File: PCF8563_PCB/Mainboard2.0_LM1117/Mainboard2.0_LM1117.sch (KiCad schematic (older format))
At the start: 40 parts, among them J1 USB_B, J2 CONN_01X03, J3 CONN_01X03, J4 CONN_01X02, J5 CONN_01X02, J6 SD_Card, Q1 BC847, Q2 BC847, SW1 SW_DIP_x01, U1 FT232RL, U2 ESP-12E, U3 PCF8563, U4 LM1117-3.3, Y1 Crystal

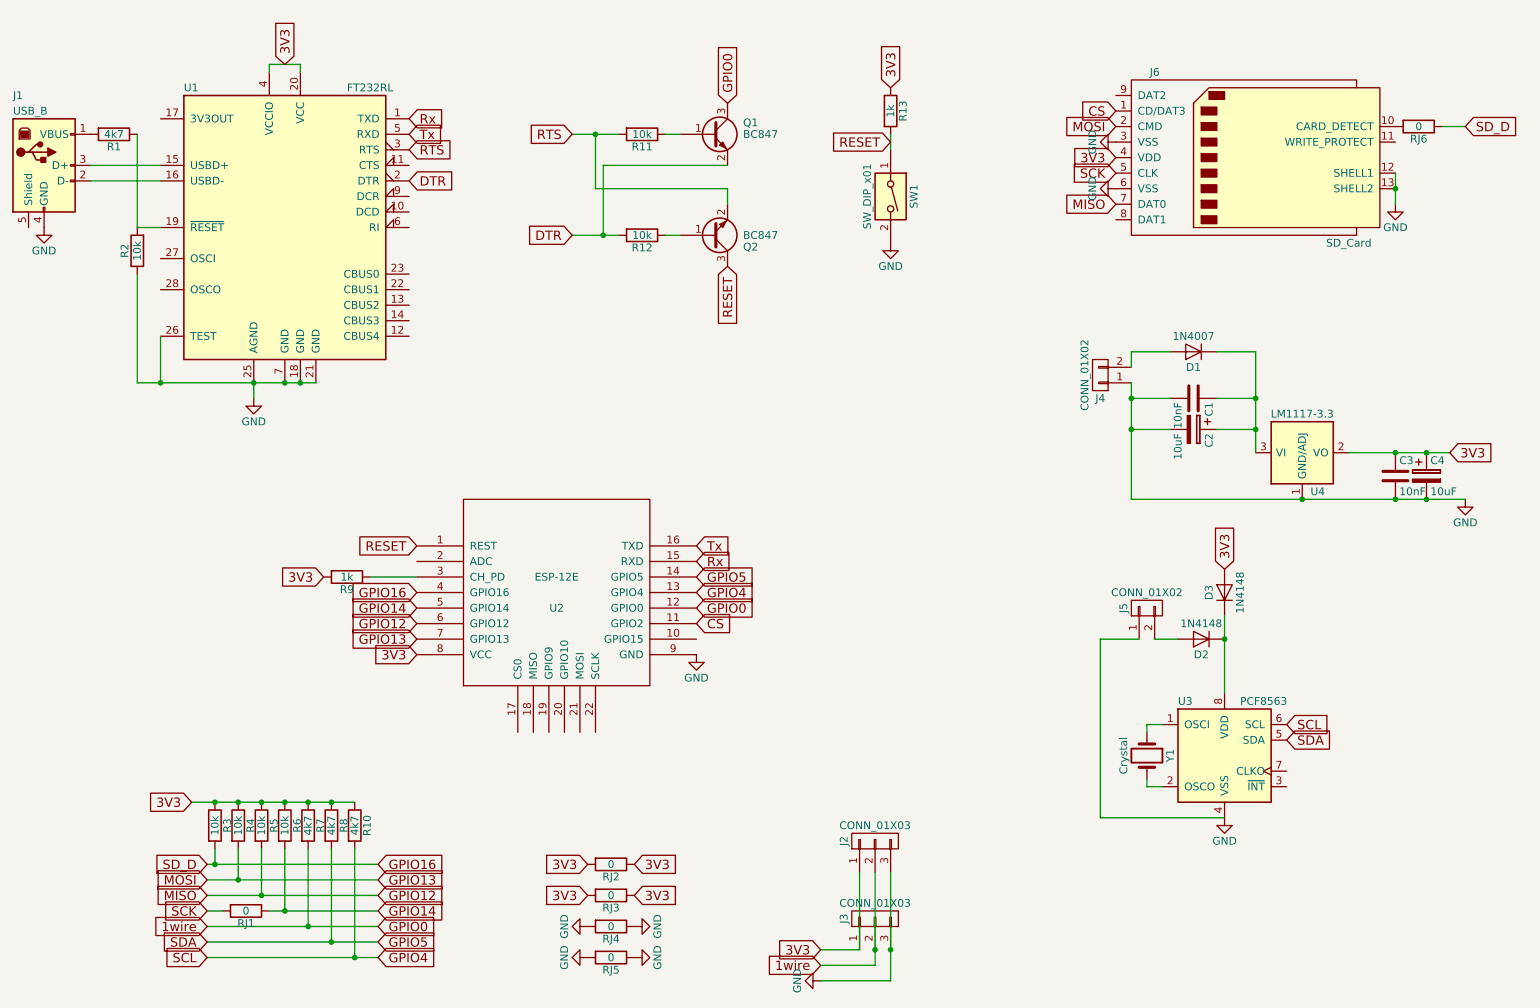
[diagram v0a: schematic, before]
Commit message: PCB work
Need to remove 1.1 files from 2.0 folder
Fixed component enumeration so PCB rework will be easier
Still need to finish new PCB
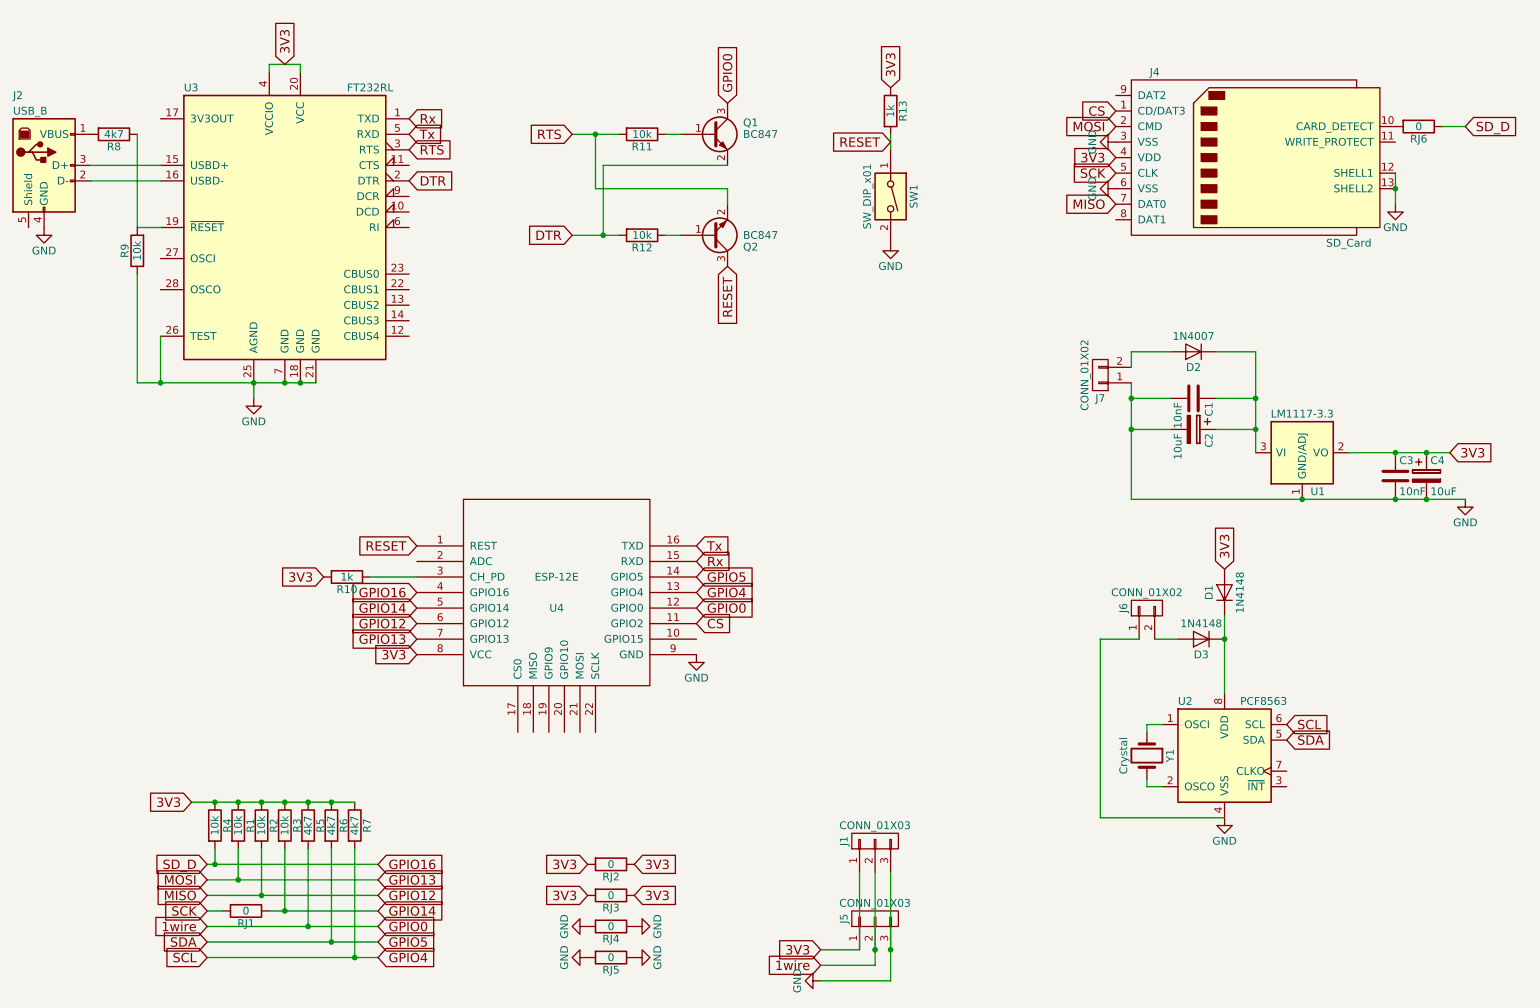
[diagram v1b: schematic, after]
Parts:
- renumbered D3 to D1, D1 to D2, D2 to D3, J2 to J1, J1 to J2, J6 to J4, J3 to J5, J5 to J6, J4 to J7, R4 to R1, R9 to R10, R5 to R2, R6 to R3, R3 to R4, R7 to R5, R8 to R6, R10 to R7, R1 to R8, R2 to R9, U4 to U1, U3 to U2, U1 to U3, U2 to U4
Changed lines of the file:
@@
 LIBS:valves
 LIBS:ESP8266
-LIBS:74xgxx
-LIBS:ac-dc
-LIBS:actel
-LIBS:allegro
-LIBS:Altera
-LIBS:analog_devices
-LIBS:battery_management
-LIBS:bbd
-LIBS:bosch
-LIBS:brooktre
-LIBS:cmos_ieee
-LIBS:dc-dc
-LIBS:diode
-LIBS:elec-unifil
-LIBS:ESD_Protection
-LIBS:ftdi
-LIBS:gennum
-LIBS:graphic_symbols
-LIBS:hc11
-LIBS:infineon
-LIBS:intersil
-LIBS:ir
-LIBS:Lattice
-LIBS:leds
-LIBS:LEM
-LIBS:maxim
-LIBS:mechanical
-LIBS:microchip_dspic33dsc
-LIBS:microchip_pic10mcu
-LIBS:microchip_pic12mcu
-LIBS:microchip_pic16mcu
-LIBS:microchip_pic18mcu
-LIBS:microchip_pic24mcu
-LIBS:microchip_pic32mcu
-LIBS:modules
-LIBS:motor_drivers
-LIBS:motors
-LIBS:msp430
-LIBS:nordicsemi
-LIBS:nxp
-LIBS:nxp_armmcu
-LIBS:onsemi
-LIBS:Oscillators
-LIBS:Power_Management
-LIBS:powerint
-LIBS:pspice
-LIBS:references
-LIBS:relays
-LIBS:rfcom
-LIBS:RFSolutions
-LIBS:sensors
-LIBS:silabs
-LIBS:stm8
-LIBS:stm32
-LIBS:supertex
-LIBS:switches
-LIBS:transf
-LIBS:triac_thyristor
-LIBS:ttl_ieee
-LIBS:video
-LIBS:wiznet
-LIBS:Worldsemi
-LIBS:Xicor
-LIBS:zetex
-LIBS:Zilog
 LIBS:Mainboard2.0_LM1117-cache
 EELAYER 25 0
@@
 GPIO16
 $Comp
-L R R7
+L R R5
 U 1 1 591DCE97
 P 2550 6200
-F 0 "R7" V 2630 6200 50  0000 C CNN
+F 0 "R5" V 2630 6200 50  0000 C CNN
 F 1 "4k7" V 2550 6200 50  0000 C CNN
 F 2 "Resistors_SMD:R_1206_HandSoldering" V 2480 6200 50  0001 C CNN
@@
 $EndComp
 $Comp
-L R R8
+L R R6
 U 1 1 591DCEFA
 P 2700 6200
-F 0 "R8" V 2780 6200 50  0000 C CNN
+F 0 "R6" V 2780 6200 50  0000 C CNN
 F 1 "4k7" V 2700 6200 50  0000 C CNN
 F 2 "Resistors_SMD:R_1206_HandSoldering" V 2630 6200 50  0001 C CNN
@@
 $EndComp
 $Comp
-L R R10
+L R R7
 U 1 1 591DCF1C
 P 2850 6200
-F 0 "R10" V 2930 6200 50  0000 C CNN
+F 0 "R7" V 2930 6200 50  0000 C CNN
 F 1 "4k7" V 2850 6200 50  0000 C CNN
 F 2 "Resistors_SMD:R_1206_HandSoldering" V 2780 6200 50  0001 C CNN
@@
 $EndComp
 $Comp
-L CONN_01X03 J3
+L CONN_01X03 J5
 U 1 1 591DD18C
 P 6200 6800
-F 0 "J3" H 6200 7000 50  0000 C CNN
+F 0 "J5" H 6200 7000 50  0000 C CNN
 F 1 "CONN_01X03" V 6300 6800 50  0000 C CNN
 F 2 "Pin_Headers:Pin_Header_Straight_1x03_Pitch2.54mm_SMD_Pin1Left" H 6200 6800 50  0001 C CNN
@@
 $EndComp
 $Comp
-L CONN_01X03 J2
+L CONN_01X03 J1
 U 1 1 591DD1E5
 P 6200 6300
-F 0 "J2" H 6200 6500 50  0000 C CNN
+F 0 "J1" H 6200 6500 50  0000 C CNN
 F 1 "CONN_01X03" V 6300 6300 50  0000 C CNN
 F 2 "Pin_Headers:Pin_Header_Straight_1x03_Pitch2.54mm_SMD_Pin1Left" H 6200 6300 50  0001 C CNN
@@
 $EndComp
 $Comp
-L SD_Card J6
+L SD_Card J4
 U 1 1 591DD53A
 P 8650 1900
-F 0 "J6" H 8000 2450 50  0000 C CNN
+F 0 "J4" H 8000 2450 50  0000 C CNN
 F 1 "SD_Card" H 9250 1350 50  0000 C CNN
 F 2 "Moje:SDCARD-STANDARD" H 8850 2250 50  0001 C CNN
@@
 MISO
 $Comp
-L R R3
+L R R4
 U 1 1 591DDBFF
 P 1950 6200
-F 0 "R3" V 2030 6200 50  0000 C CNN
+F 0 "R4" V 2030 6200 50  0000 C CNN
 F 1 "10k" V 1950 6200 50  0000 C CNN
 F 2 "Resistors_SMD:R_1206_HandSoldering" V 1880 6200 50  0001 C CNN
@@
 SD_D
 $Comp
-L R R4
+L R R1
 U 1 1 591DE219
 P 2100 6200
-F 0 "R4" V 2180 6200 50  0000 C CNN
+F 0 "R1" V 2180 6200 50  0000 C CNN
 F 1 "10k" V 2100 6200 50  0000 C CNN
 F 2 "Resistors_SMD:R_1206_HandSoldering" V 2030 6200 50  0001 C CNN
@@
 $EndComp
 $Comp
-L R R5
+L R R2
 U 1 1 591DE506
 P 2250 6200
-F 0 "R5" V 2330 6200 50  0000 C CNN
+F 0 "R2" V 2330 6200 50  0000 C CNN
 F 1 "10k" V 2250 6200 50  0000 C CNN
 F 2 "Resistors_SMD:R_1206_HandSoldering" V 2180 6200 50  0001 C CNN
@@
 $EndComp
 $Comp
-L R R6
+L R R3
 U 1 1 591DE541
 P 2400 6200
-F 0 "R6" V 2480 6200 50  0000 C CNN
+F 0 "R3" V 2480 6200 50  0000 C CNN
 F 1 "10k" V 2400 6200 50  0000 C CNN
 F 2 "Resistors_SMD:R_1206_HandSoldering" V 2330 6200 50  0001 C CNN
@@
 3V3
 $Comp
-L PCF8563 U3
+L PCF8563 U2
 U 1 1 591DECCB
 P 8450 5750
-F 0 "U3" H 8150 6100 50  0000 L CNN
+F 0 "U2" H 8150 6100 50  0000 L CNN
 F 1 "PCF8563" H 8550 6100 50  0000 L CNN
 F 2 "Housings_SOIC:SOIC-8_3.9x4.9mm_Pitch1.27mm" H 8450 5750 50  0001 C CNN
@@
 $EndComp
 $Comp
-L D D2
+L D D3
 U 1 1 591DF21A
 P 8300 5000
-F 0 "D2" H 8300 5100 50  0000 C CNN
+F 0 "D3" H 8300 5100 50  0000 C CNN
 F 1 "1N4148" H 8300 4900 50  0000 C CNN
 F 2 "Diodes_SMD:D_MiniMELF" H 8300 5000 50  0001 C CNN
@@
 $EndComp
 $Comp
-L D D3
+L D D1
 U 1 1 591DF401
 P 8450 4700
-F 0 "D3" H 8450 4800 50  0000 C CNN
+F 0 "D1" H 8450 4800 50  0000 C CNN
 F 1 "1N4148" H 8450 4600 50  0000 C CNN
 F 2 "Diodes_SMD:D_MiniMELF" H 8450 4700 50  0001 C CNN
@@
 $EndComp
 $Comp
-L LM1117-3.3-RESCUE-Mainboard2.0_LM1117 U4
+L LM1117-3.3-RESCUE-Mainboard2.0_LM1117 U1
 U 1 1 591E00AF
 P 8950 3800
-F 0 "U4" H 9050 3550 50  0000 C CNN
+F 0 "U1" H 9050 3550 50  0000 C CNN
 F 1 "LM1117-3.3" H 8950 4050 50  0000 C CNN
 F 2 "TO_SOT_Packages_SMD:SOT-223-3Lead_TabPin2" H 8950 3800 50  0001 C CNN
@@
 $EndComp
 $Comp
-L D D1
+L D D2
 U 1 1 591E10E9
 P 8250 3150
-F 0 "D1" H 8250 3250 50  0000 C CNN
+F 0 "D2" H 8250 3250 50  0000 C CNN
 F 1 "1N4007" H 8250 3050 50  0000 C CNN
 F 2 "Diodes_SMD:D_SMA" H 8250 3150 50  0001 C CNN
@@
 $EndComp
 $Comp
-L CONN_01X02 J5
+L CONN_01X02 J6
 U 1 1 591E39F7
 P 7950 4800
-F 0 "J5" H 7950 4950 50  0000 C CNN
+F 0 "J6" H 7950 4950 50  0000 C CNN
 F 1 "CONN_01X02" V 8050 4800 50  0000 C CNN
 F 2 "Pin_Headers:Pin_Header_Straight_1x02_Pitch2.54mm_SMD_Pin1Left" H 7950 4800 50  0001 C CNN
@@
 $EndComp
 $Comp
-L CONN_01X02 J4
+L CONN_01X02 J7
 U 1 1 591F80FA
 P 7650 3300
-F 0 "J4" H 7650 3450 50  0000 C CNN
+F 0 "J7" H 7650 3450 50  0000 C CNN
 F 1 "CONN_01X02" V 7750 3300 50  0000 C CNN
 F 2 "Pin_Headers:Pin_Header_Straight_1x02_Pitch2.54mm_SMD_Pin1Left" H 7650 3300 50  0001 C CNN
@@
 Connection ~ 8950 4100
 $Comp
-L ESP-12E U2
+L ESP-12E U4
 U 1 1 59610456
 P 4150 4700
-F 0 "U2" H 4150 4600 50  0000 C CNN
+F 0 "U4" H 4150 4600 50  0000 C CNN
 F 1 "ESP-12E" H 4150 4800 50  0000 C CNN
 F 2 "ESP8266:ESP-12E_SMD" H 4150 4700 50  0001 C CNN
@@
 	8400 3150 8650 3150
 $Comp
-L FT232RL U1
+L FT232RL U3
 U 1 1 59610C09
 P 2400 2350
-F 0 "U1" H 1750 3250 50  0000 L CNN
+F 0 "U3" H 1750 3250 50  0000 L CNN
 F 1 "FT232RL" H 2800 3250 50  0000 L CNN
 F 2 "Housings_SSOP:SSOP-28_5.3x10.2mm_Pitch0.65mm" H 2400 2350 50  0001 C CNN
@@
 Rx
 $Comp
-L USB_B J1
+L USB_B J2
 U 1 1 596132B0
 P 850 1950
-F 0 "J1" H 650 2400 50  0000 L CNN
+F 0 "J2" H 650 2400 50  0000 L CNN
 F 1 "USB_B" H 650 2300 50  0000 L CNN
 F 2 "Connectors:USB_Micro-B" H 1000 1900 50  0001 C CNN
@@
 	2500 1300 2500 1350
 $Comp
-L R R1
+L R R8
 U 1 1 59616677
 P 1300 1750
-F 0 "R1" V 1380 1750 50  0000 C CNN
+F 0 "R8" V 1380 1750 50  0000 C CNN
 F 1 "4k7" V 1300 1750 50  0000 C CNN
 F 2 "Resistors_SMD:R_1206_HandSoldering" V 1230 1750 50  0001 C CNN
@@
 $EndComp
 $Comp
-L R R2
+L R R9
 U 1 1 596168C6
 P 1450 2500
-F 0 "R2" V 1530 2500 50  0000 C CNN
+F 0 "R9" V 1530 2500 50  0000 C CNN
 F 1 "10k" V 1450 2500 50  0000 C CNN
 F 2 "Resistors_SMD:R_1206_HandSoldering" V 1380 2500 50  0001 C CNN
@@
 Connection ~ 1600 3350
 $Comp
-L R R9
+L R R10
 U 1 1 59617D63
 P 2800 4600
-F 0 "R9" V 2880 4600 50  0000 C CNN
+F 0 "R10" V 2880 4600 50  0000 C CNN
 F 1 "1k" V 2800 4600 50  0000 C CNN
 F 2 "Resistors_SMD:R_1206_HandSoldering" V 2730 4600 50  0001 C CNN

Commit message: SMD board complete
Full SMD board is complete - needs to be tested though. Looks kinda awful, large SD card slot is taking lots of space.
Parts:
- removed Q1, Q2: BC847, TO_SOT_Packages_SMD:SOT-23, symbol BC847
- removed R11: 10k, Resistors_SMD:R_1206_HandSoldering, symbol R
- removed RJ3, RJ4, RJ5, RJ6: 0, Resistors_SMD:R_1206_HandSoldering, symbol R
- added SW2: FLASH, Buttons_Switches_SMD:SW_DIP_x1_W5.08mm_Slide_Copal_CHS-A, symbol SW_DIP_x01
- J4: footprint Moje:SDCARD-STANDARD -> dodatki:SDCARD-STANDARD
- R12: value 10k -> 1k
- RJ1, RJ2: footprint Resistors_SMD:R_1206_HandSoldering -> Resistors_SMD:R_1206
- SW1: value SW_DIP_x01 -> RESET
- Y1: footprint Crystals:Crystal_AT310_d3.0mm_l10.0mm_Horizontal -> Crystals:Crystal_SMD_SeikoEpson_MC406-4pin_9.6x4.1mm
- renumbered R13 to R11
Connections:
- net 1wire: now also R12.2, SW2.1
- net 3V3: now also R12.1; no longer RJ2.1, RJ2.2
- net GND: now also RJ2.1, RJ2.2, SW2.2
- net GPIO14: now also J4.5 (CLK); no longer RJ1.1
- net at J4.10 (CARD_DETECT): now also RJ1.2
- net DTR: no longer names the net of U3.2 (DTR)
- net DTR: no longer R12.2
- net GPIO16 renamed SD_D
- net SD_D: now also RJ1.1
- net RTS: no longer names the net of U3.3 (RTS)
- removed net SCK: J4.5 (CLK), RJ1.2
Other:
- note added: "91SMX(IQD)/MC406(seiko epson)\ncrystals can be used"
- moved on the sheet: J1, J5, R1, R10, R11, R2, R3, R4, R5, R6, R7, SW1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
